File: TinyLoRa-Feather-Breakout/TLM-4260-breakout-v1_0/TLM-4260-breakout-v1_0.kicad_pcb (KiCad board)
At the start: 4 copper layers, 22.9 x 50.8 mm, 60 parts, among them J1 U.FL-R-SMT-1, J2 SMA-Edge-Mount, J3 USB_C_Receptacle_USB2.0, J4 JST_PH, J5 Conn_ARM_JTAG_SWD_10, Q1 SI2323DS, SW1 USR_BTN, SW2 RESET, U1 MCP73831, U2 ME6215C33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

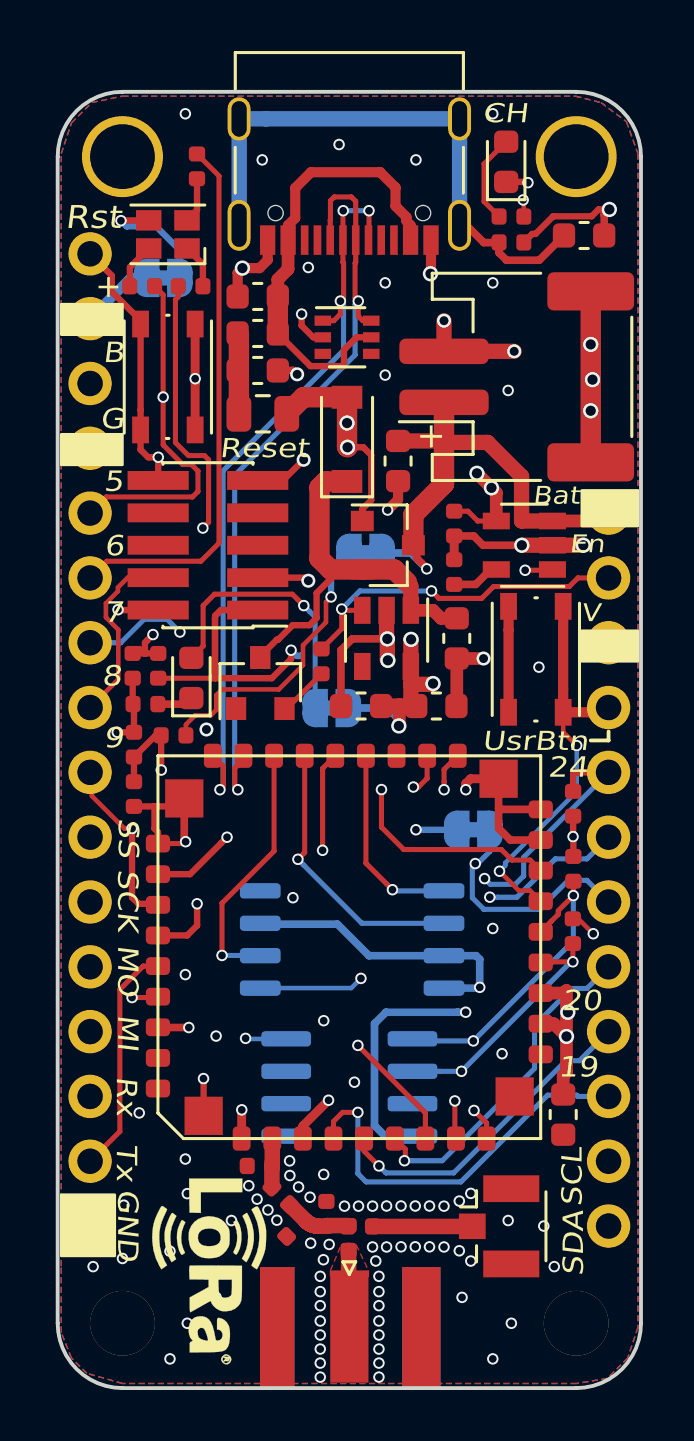
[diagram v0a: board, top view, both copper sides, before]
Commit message: Latest version of TinyLoRa 4260
Slight layout updates and added BOM
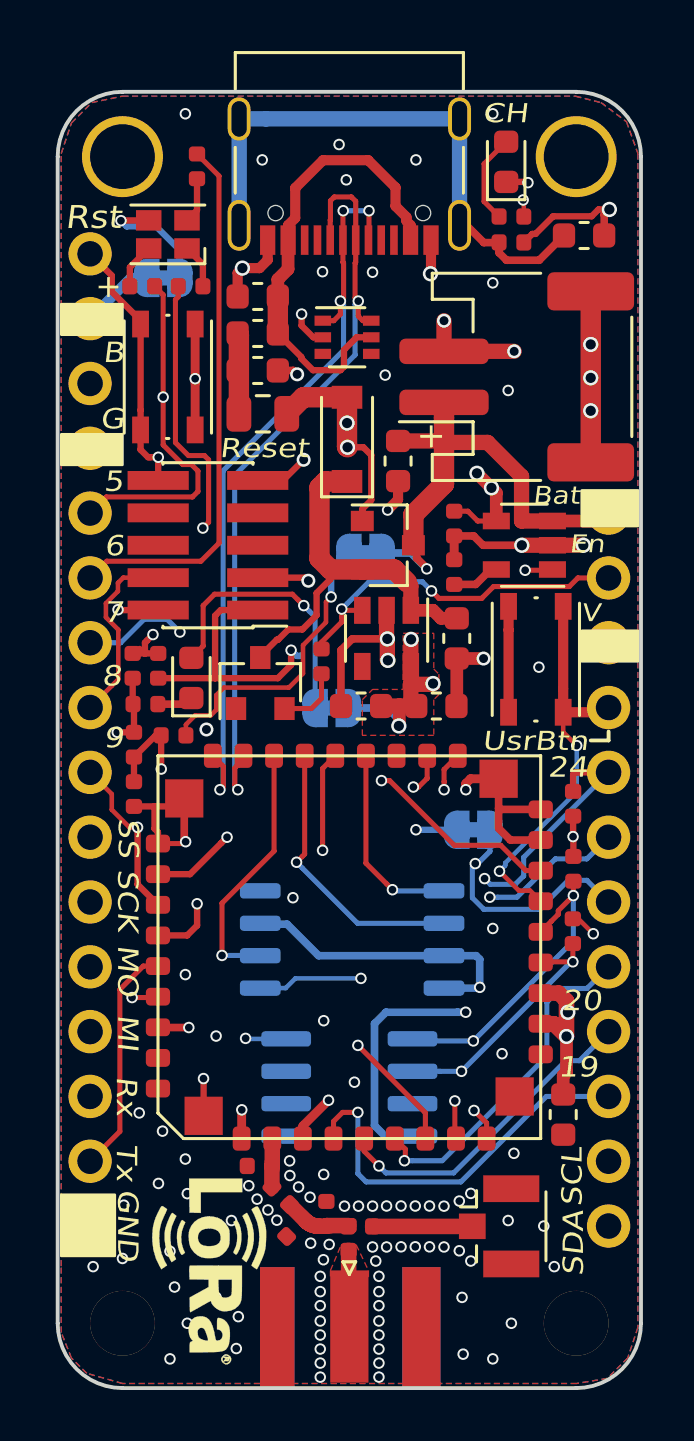
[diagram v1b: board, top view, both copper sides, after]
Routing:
- net +3V3: track 67.5 -> 64.5 mm
- net (no net): track 13.5 -> 11.4 mm
- net PA09_AIN1: track 18.2 -> 16.5 mm
- net PA18_TX3: track 47.1 -> 48.6 mm
- net PA14: track 45.4 -> 44.5 mm
- net PA19_RX3: track 35.9 -> 35.2 mm
- net /Vin: track 17.8 -> 18.3 mm
- net Net-(R3-Pad2): track 2.02 -> 2.58 mm
- net GND: vias 106 -> 114
- added copper zone on F.Cu, net +3V3

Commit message: TinyLoRa 4260 slight layout changes
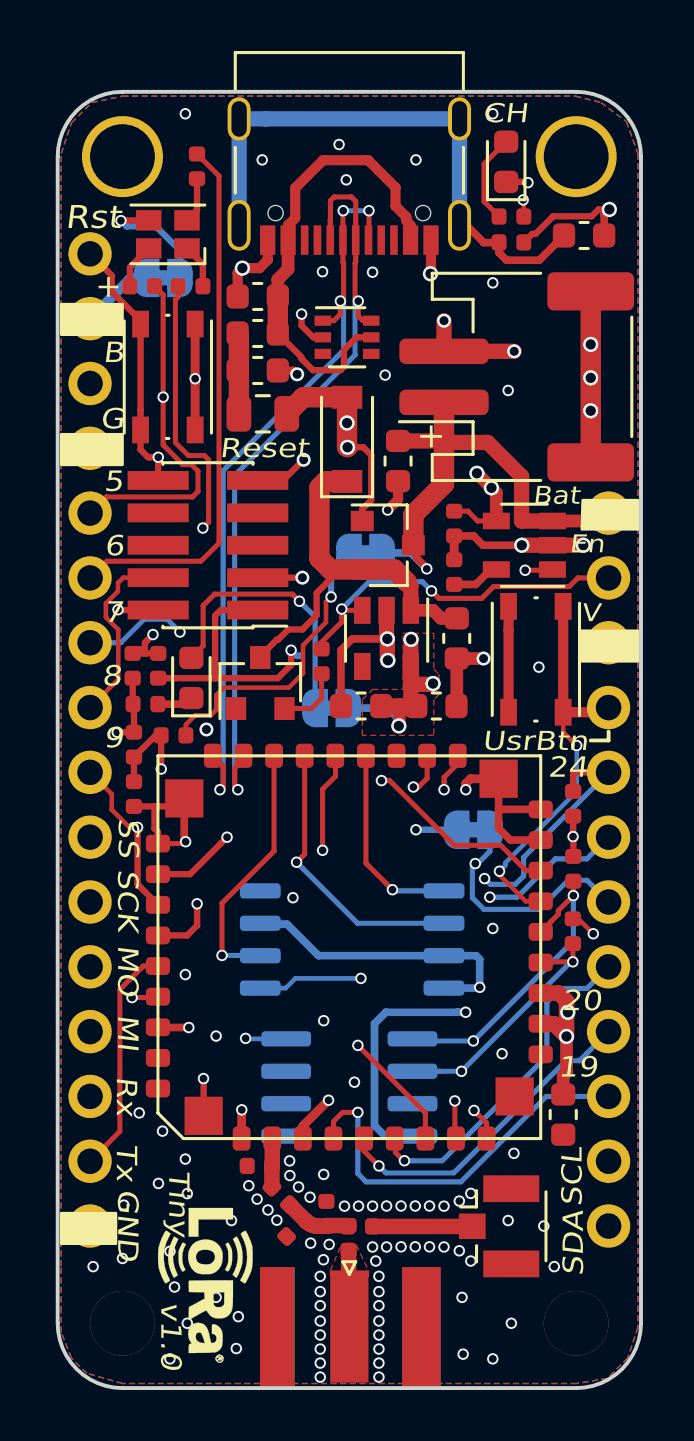
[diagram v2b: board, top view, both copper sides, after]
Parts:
- removed the G*** at (130.4, 114.8)
- added G***: LOGO, Custom_Logos:Lora-5, F.Cu at (130.2, 115.3)
- moved REF** 1.35 mm to (131.1, 85.8)
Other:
- board text added: "21"
- board text added: "22"
- board text added: "23"
- board text added: "25"
- board text added: "3V"
- board text added: "BCKP"
- board text added: "MISO"
- board text added: "MOSI"
- board text added: "Tiny"
- board text added: "VBAT"
- board text added: "VBUS"
- board text added: "open hardware"
- board text added: "v1.0"
